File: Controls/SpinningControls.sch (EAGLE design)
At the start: 120 parts, among them IC1 S-19246E33H-V5T2U, IC2 SN74LVC1G34DBVR, IC3 SN74LVC1G34DBVR, IC4 SN74LVC1G34DBVR, IC5 TXS0104EDR, J10 SULLINS_PPPC062LFBN-RCSULLINS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, J11 SULLINS_PPPC062LFBN-RCSULLINS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, J12 SULLINS_PPPC062LFBN-RCSULLINS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, J13 SULLINS_PPPC062LFBN-RCSULLINS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, J14 SULLINS_PPPC062LFBN-RCSULLINS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

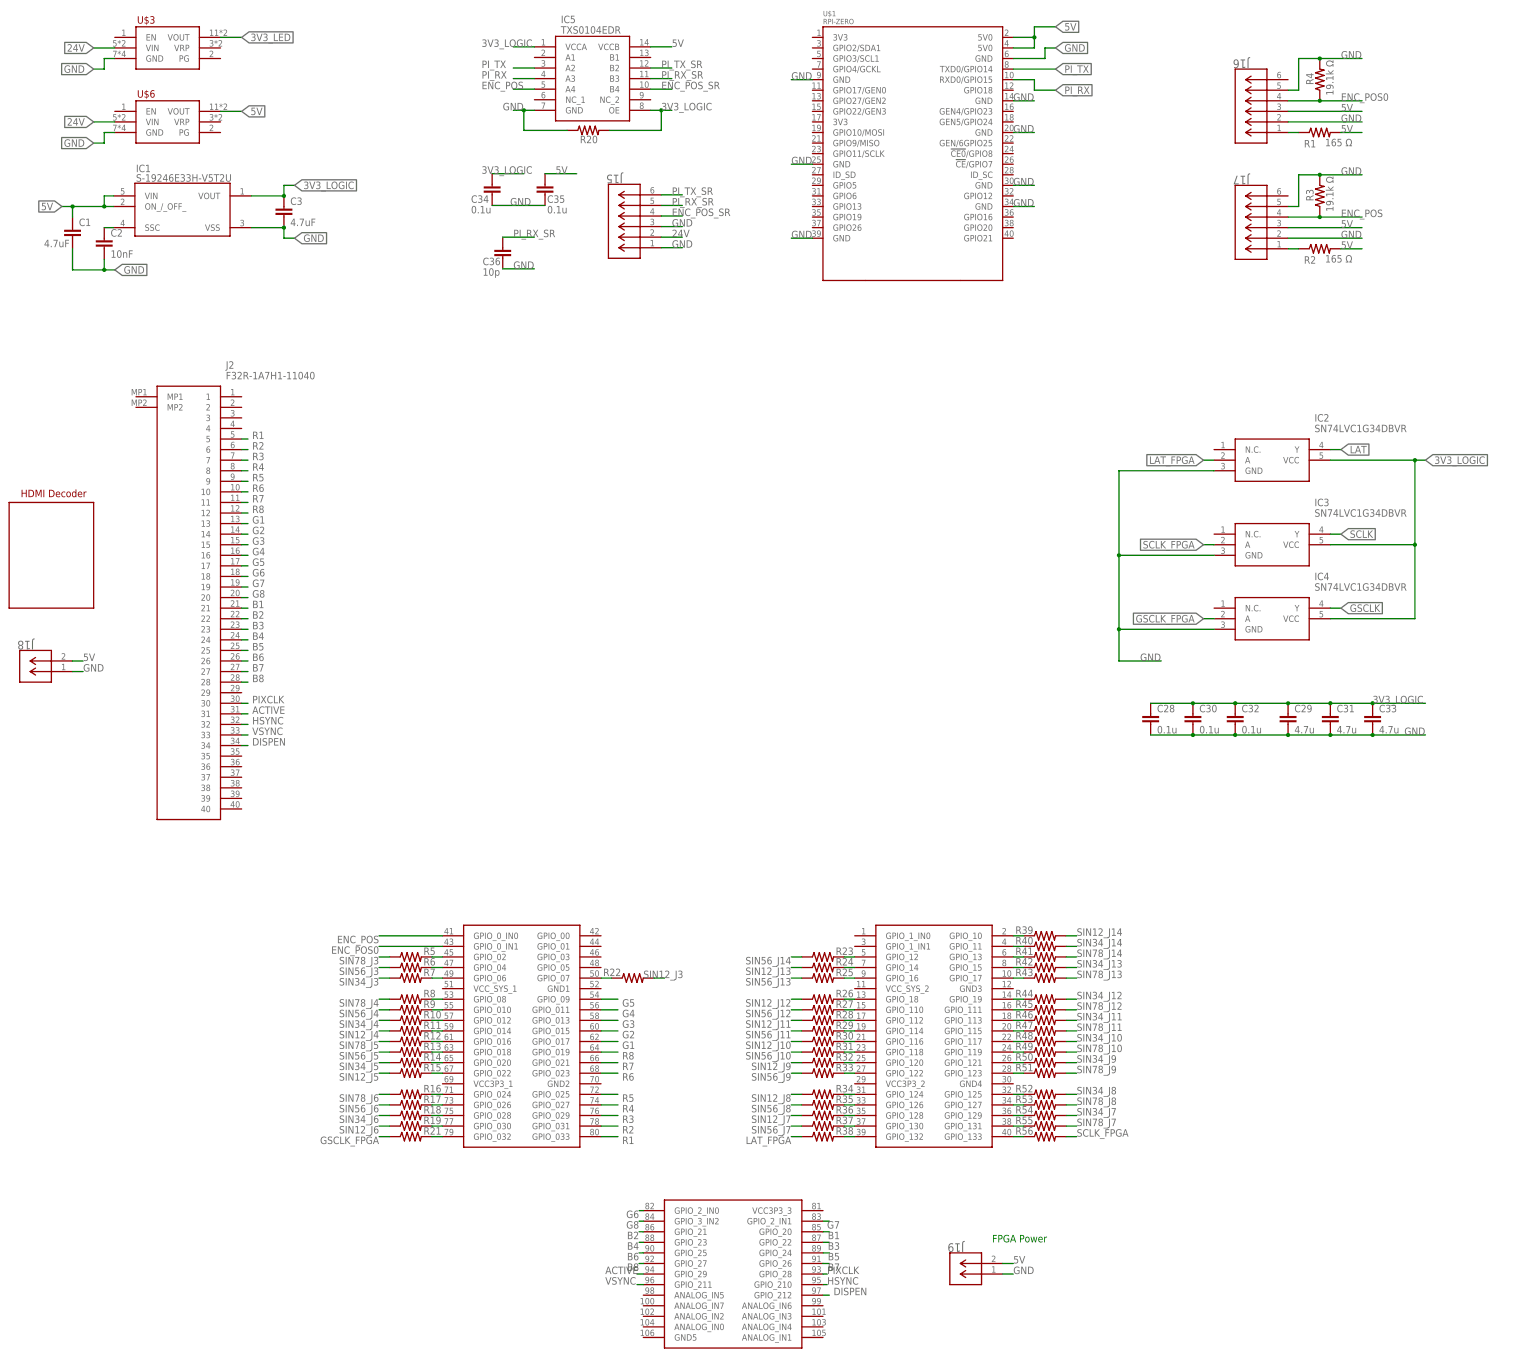
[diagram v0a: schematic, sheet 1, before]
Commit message: dan tings, 50ohm FPGA inline, 3v3 to 5 logic for SR
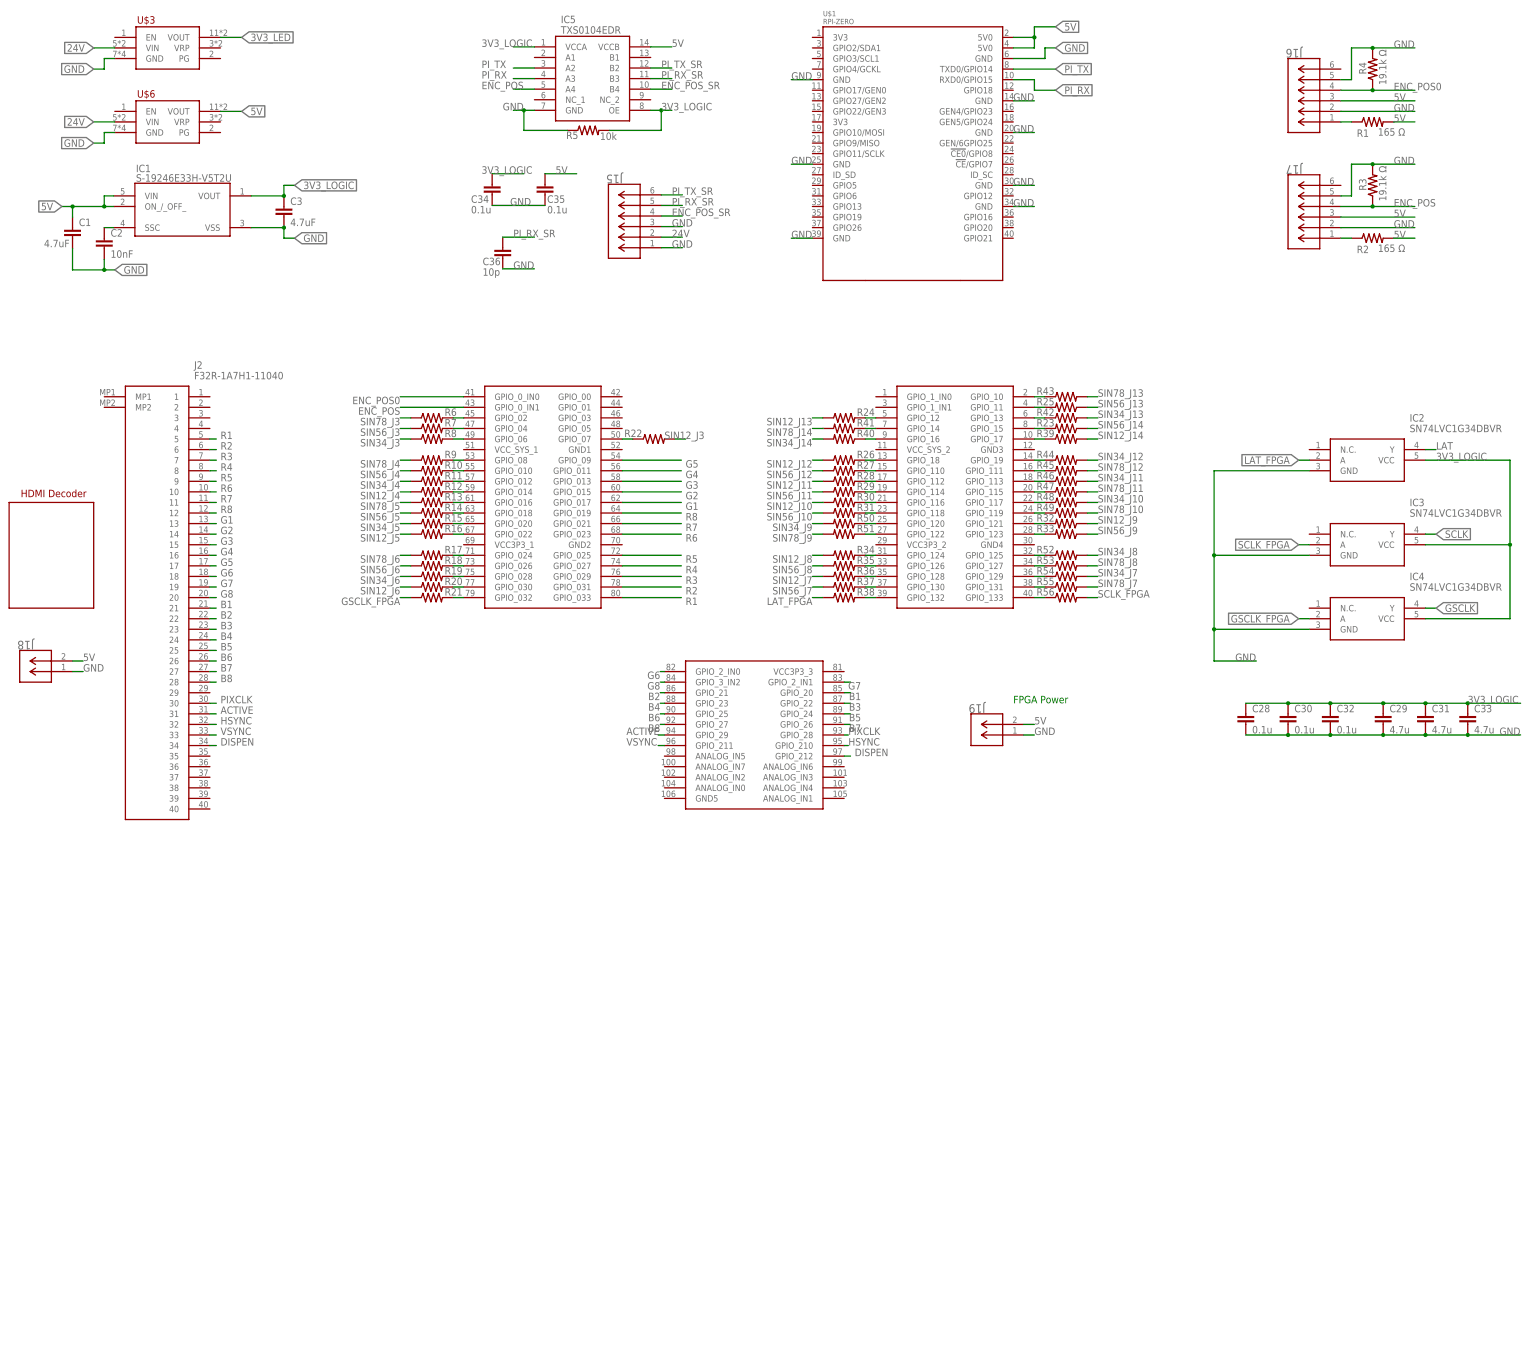
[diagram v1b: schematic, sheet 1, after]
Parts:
- R20: device rcl:R-US_R0603 -> rcl:R-US_R0402
- R5: value (none) -> 10k; device rcl:R-US_R0402 -> rcl:R-US_R0603
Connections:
- net 3V3_LOGIC: now also R5.2; no longer R20.2
- net ENC_POS: now also FPGA.GPIO_0_IN1; no longer FPGA.GPIO_0_IN0
- net ENC_POS0: now also FPGA.GPIO_0_IN0; no longer FPGA.GPIO_0_IN1
- net GND: now also R5.1; no longer R20.1
- net N$10: now also FPGA.GPIO_16; no longer FPGA.GPIO_11
- net N$11: now also FPGA.GPIO_14; no longer FPGA.GPIO_13
- net N$12: now also FPGA.GPIO_13; no longer FPGA.GPIO_15
- net N$13: now also FPGA.GPIO_10; no longer FPGA.GPIO_17
- net N$15: now also R7.2; no longer R6.2
- net N$16: now also R8.2; no longer R7.2
- net N$18: now also R9.2; no longer R8.2
- net N$19: now also R10.2; no longer R9.2
- net N$2: now also R6.2; no longer R5.2
- net N$20: now also R11.2; no longer R10.2
- net N$21: now also R12.2; no longer R11.2
- net N$22: now also R13.2; no longer R12.2
- net N$23: now also R14.2; no longer R13.2
- net N$24: now also R15.2; no longer R14.2
- net N$25: now also R16.2; no longer R15.2
- net N$27: now also R17.2; no longer R16.2
- net N$28: now also R18.2; no longer R17.2
- net N$29: now also R19.2; no longer R18.2
- net N$30: now also R20.2; no longer R19.2
- net N$34: now also FPGA.GPIO_121; no longer FPGA.GPIO_120
- net N$35: now also FPGA.GPIO_123; no longer FPGA.GPIO_122
- net N$47: now also FPGA.GPIO_120; no longer FPGA.GPIO_121
- net N$48: now also FPGA.GPIO_122; no longer FPGA.GPIO_123
- net N$54: now also FPGA.GPIO_17; no longer FPGA.GPIO_10
- net N$7: now also FPGA.GPIO_15; no longer FPGA.GPIO_12
- net N$8: now also FPGA.GPIO_12; no longer FPGA.GPIO_14
- net N$9: now also FPGA.GPIO_11; no longer FPGA.GPIO_16
- net SIN12_J4: now also R12.1; no longer R11.1
- net SIN12_J5: now also R16.1; no longer R15.1
- net SIN12_J6: now also R20.1; no longer R19.1
- net SIN34_J3: now also R8.1; no longer R7.1
- net SIN34_J4: now also R11.1; no longer R10.1
- net SIN34_J5: now also R15.1; no longer R14.1
- net SIN34_J6: now also R19.1; no longer R18.1
- net SIN56_J3: now also R7.1; no longer R6.1
- net SIN56_J4: now also R10.1; no longer R9.1
- net SIN56_J5: now also R14.1; no longer R13.1
- net SIN56_J6: now also R18.1; no longer R17.1
- net SIN78_J3: now also R6.1; no longer R5.1
- net SIN78_J4: now also R9.1; no longer R8.1
- net SIN78_J5: now also R13.1; no longer R12.1
- net SIN78_J6: now also R17.1; no longer R16.1
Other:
- moved on the sheet: C28, C29, C30, C31, C32, C33, IC2, IC3, IC4, J16, J17, J19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

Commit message: full routing layout and schematic
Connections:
- net N$34: now also FPGA.GPIO_120; no longer FPGA.GPIO_121
- net N$35: now also FPGA.GPIO_122; no longer FPGA.GPIO_123
- net N$39: now also FPGA.GPIO_131; no longer FPGA.GPIO_130
- net N$47: now also FPGA.GPIO_121; no longer FPGA.GPIO_120
- net N$48: now also FPGA.GPIO_123; no longer FPGA.GPIO_122
- net N$52: now also FPGA.GPIO_130; no longer FPGA.GPIO_131
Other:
- moved on the sheet: R32, R33, R37, R50, R51, R55
